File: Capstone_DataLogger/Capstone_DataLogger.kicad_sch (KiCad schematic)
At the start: 0 parts

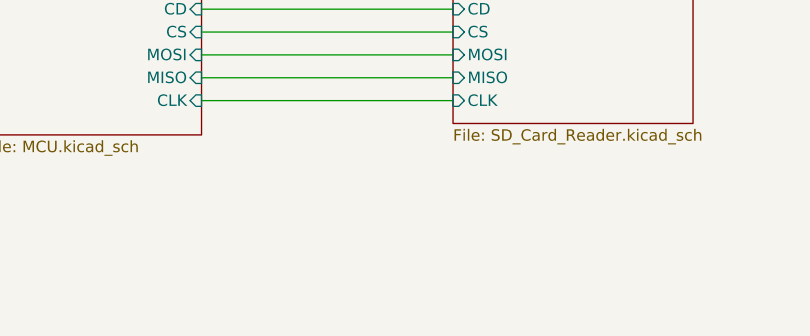
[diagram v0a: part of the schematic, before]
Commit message: added resistor
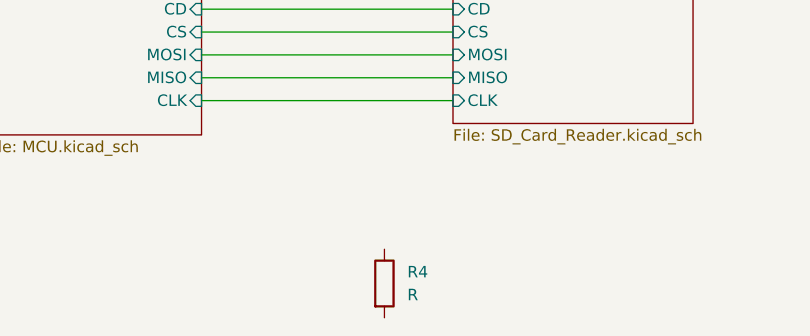
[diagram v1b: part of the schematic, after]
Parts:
- added R4: R, symbol Device:R
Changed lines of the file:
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@@
+		)
+	)
+	(symbol
+		(lib_id "Device:R")
+		(at 170.18 129.54 0)
+		(unit 1)
+		(exclude_from_sim no)
+		(in_bom yes)
+		(on_board yes)
+		(dnp no)
+		(fields_autoplaced yes)
+		(property "Reference" "R4"
+			(at 172.72 128.2699 0)
+			(effects
+				(font
+					(size 1.27 1.27)
+				)
+				(justify left)
+			)
+		)
+		(property "Value" "R"
+			(at 172.72 130.8099 0)
+			(effects
+				(font
+					(size 1.27 1.27)
+				)
+				(justify left)
+			)
+		)
+		(property "Footprint" ""
+			(at 168.402 129.54 90)
+			(effects
+				(font
+					(size 1.27 1.27)
+				)
+				(hide yes)
+			)
+		)
+		(property "Datasheet" "~"
+			(at 170.18 129.54 0)
+			(effects
+				(font
+					(size 1.27 1.27)
+				)
+				(hide yes)
+			)
+		)
+		(property "Description" "Resistor"
+			(at 170.18 129.54 0)
+			(effects
+				(font
+					(size 1.27 1.27)
+				)
+				(hide yes)
+			)
+		)
+		(pin "2"
+		)
+		(pin "1"
+		)
+		(instances
+			(project ""
+				(path "/3b56a84b-c06c-4c22-a01a-903db63bf091"
+					(reference "R4")
+					(unit 1)
+				)
+			)
 		)
 	)

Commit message: basic changes
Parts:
- removed R4: R, symbol Device:R
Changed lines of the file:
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@@
-		)
-	)
-	(symbol
-		(lib_id "Device:R")
-		(at 170.18 129.54 0)
-		(unit 1)
-		(exclude_from_sim no)
-		(in_bom yes)
-		(on_board yes)
-		(dnp no)
-		(fields_autoplaced yes)
-		(property "Reference" "R4"
-			(at 172.72 128.2699 0)
-			(effects
-				(font
-					(size 1.27 1.27)
-				)
-				(justify left)
-			)
-		)
-		(property "Value" "R"
-			(at 172.72 130.8099 0)
-			(effects
-				(font
-					(size 1.27 1.27)
-				)
-				(justify left)
-			)
-		)
-		(property "Footprint" ""
-			(at 168.402 129.54 90)
-			(effects
-				(font
-					(size 1.27 1.27)
-				)
-				(hide yes)
-			)
-		)
-		(property "Datasheet" "~"
-			(at 170.18 129.54 0)
-			(effects
-				(font
-					(size 1.27 1.27)
-				)
-				(hide yes)
-			)
-		)
-		(property "Description" "Resistor"
-			(at 170.18 129.54 0)
-			(effects
-				(font
-					(size 1.27 1.27)
-				)
-				(hide yes)
-			)
-		)
-		(pin "2"
-		)
-		(pin "1"
-		)
-		(instances
-			(project ""
-				(path "/3b56a84b-c06c-4c22-a01a-903db63bf091"
-					(reference "R4")
-					(unit 1)
-				)
-			)
 		)
 	)
